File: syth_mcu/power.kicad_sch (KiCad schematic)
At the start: 31 parts, among them U3 AMS1117-3.3, U4 AMS1117-3.3

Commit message: All traces, no drc runs yet
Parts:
- U3, U4: footprint Package_TO_SOT_SMD:SOT-223-3_TabPin2 -> Package_TO_SOT_SMD:TO-252-3_TabPin2
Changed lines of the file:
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@@
 			)
 		)
-		(property "Footprint" "Package_TO_SOT_SMD:SOT-223-3_TabPin2"
+		(property "Footprint" "Package_TO_SOT_SMD:TO-252-3_TabPin2"
 			(at 46.99 105.41 0)
 			(hide yes)
@@
 			)
 		)
-		(property "Footprint" "Package_TO_SOT_SMD:SOT-223-3_TabPin2"
+		(property "Footprint" "Package_TO_SOT_SMD:TO-252-3_TabPin2"
 			(at 46.99 76.2 0)
 			(hide yes)

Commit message: Fixes from review 2
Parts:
- F1, F2: footprint Capacitor_THT:C_Disc_D5.1mm_W3.2mm_P5.00mm -> synth:RXEF040
- F3: footprint Capacitor_THT:C_Disc_D5.1mm_W3.2mm_P5.00mm -> synth:RXEF160
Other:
- note added: "AMS1 used for mux, and pot into gpio is neglegible, thus max current pulled is 50mA"
- note removed: "AMS1 used for mux, and pot into gpio is neglegible, thus max current pulled is 168mA"
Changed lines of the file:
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@@
 		)
 	)
-	(text "AMS1 used for mux,\nand pot into gpio is neglegible,\nthus max current pulled is 168mA"
+	(text "AMS1 used for mux,\nand pot into gpio is neglegible,\nthus max current pulled is 50mA"
 		(exclude_from_sim no)
 		(at 104.394 83.058 0)
@@
 			)
 		)
-		(property "Footprint" "Capacitor_THT:C_Disc_D5.1mm_W3.2mm_P5.00mm"
+		(property "Footprint" "synth:RXEF040"
 			(at 69.85 80.01 0)
 			(hide yes)
@@
 			)
 		)
-		(property "Footprint" "Capacitor_THT:C_Disc_D5.1mm_W3.2mm_P5.00mm"
+		(property "Footprint" "synth:RXEF160"
 			(at 60.96 25.4 0)
 			(hide yes)
@@
 			)
 		)
-		(property "Footprint" "Capacitor_THT:C_Disc_D5.1mm_W3.2mm_P5.00mm"
+		(property "Footprint" "synth:RXEF040"
 			(at 68.58 109.22 0)
 			(hide yes)

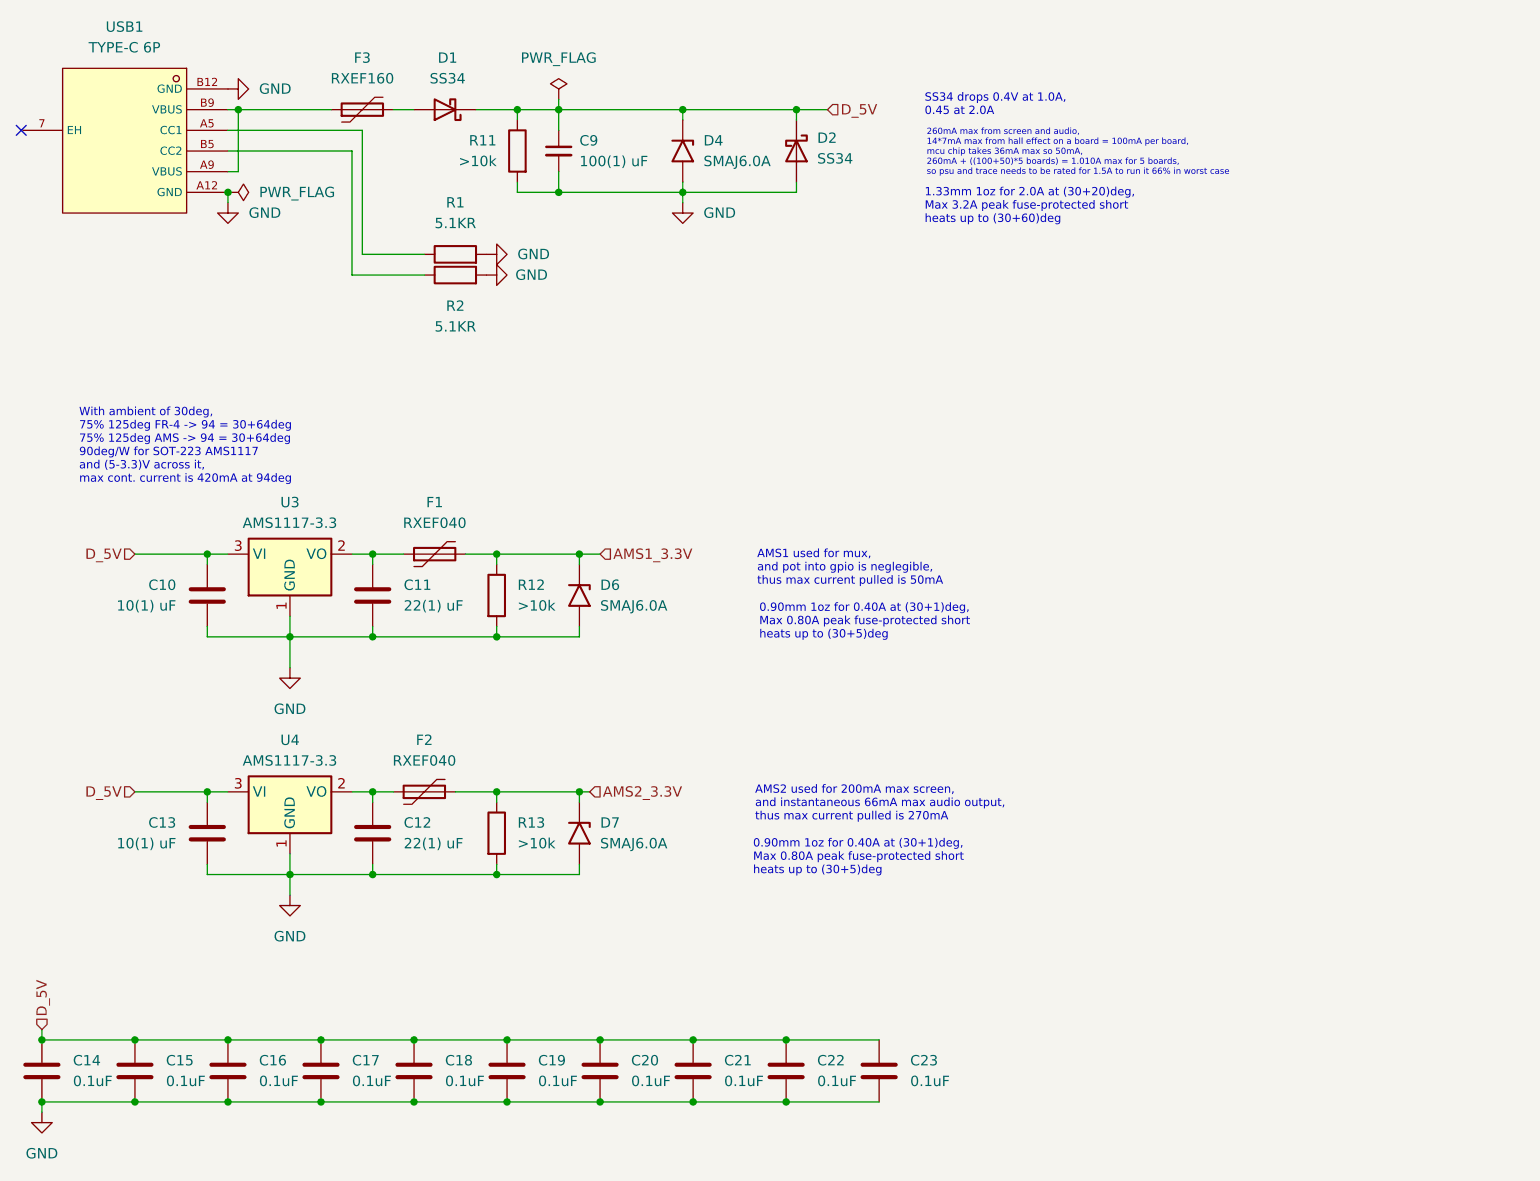
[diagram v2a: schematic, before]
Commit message: Unity-gain audio, merge AMS, 12 pots to mux, revs, footprint
Footprints:
- RXEF fuses with 1x dimension silkscreen and +0.2mm courtyard
- AMS1117 with 0.5mm minimum soldering space on all sides
- SS12D10 wider pins and add courtyard
- Changed orientation of AH3503 TO-92 to match datasheet
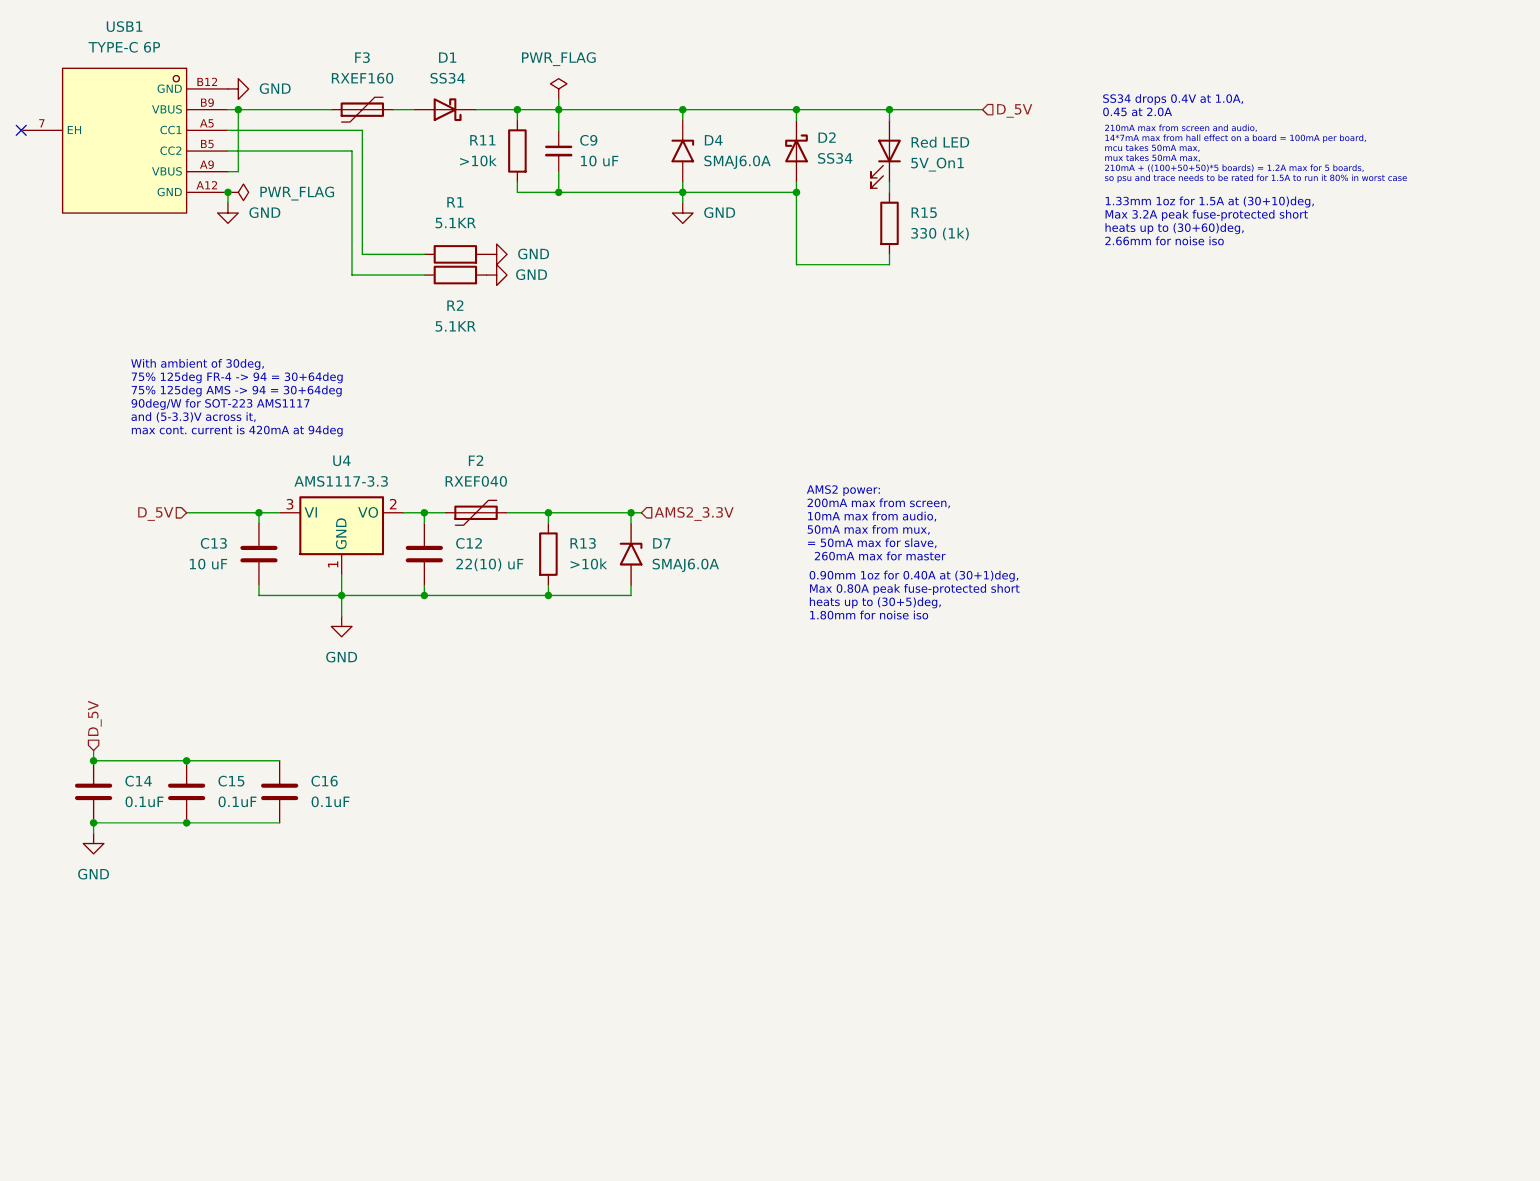
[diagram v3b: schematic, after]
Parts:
- removed C10: 10(1) uF, Capacitor_THT:C_Disc_D5.0mm_W2.5mm_P5.00mm, symbol Device:C
- removed C11: 22(1) uF, Capacitor_THT:C_Disc_D5.0mm_W2.5mm_P5.00mm, symbol Device:C
- removed C17, C18, C19, C20, C21, C22, C23: 0.1uF, Capacitor_THT:C_Disc_D5.0mm_W2.5mm_P5.00mm, symbol Device:C
- removed D6: SMAJ6.0A, Diode_SMD:D_SMA, symbol Diode:SMAJ5.0A
- removed F1: RXEF040, synth:RXEF040, symbol Device:Polyfuse
- removed R12: >10k, Resistor_THT:R_Axial_DIN0207_L6.3mm_D2.5mm_P10.16mm_Horizontal, symbol Device:R
- removed U3: AMS1117-3.3, Package_TO_SOT_SMD:TO-252-3_TabPin2, symbol Regulator_Linear:AMS1117-3.3
- added 5V_On1: Red LED, LED_THT:LED_D3.0mm, symbol Device:LED
- added R15: 330 (1k), Resistor_THT:R_Axial_DIN0207_L6.3mm_D2.5mm_P10.16mm_Horizontal, symbol Device:R
- C12: value 22(1) uF -> 22(10) uF; footprint Capacitor_THT:C_Disc_D5.0mm_W2.5mm_P5.00mm -> Capacitor_THT:CP_Radial_D4.0mm_P2.00mm
- C13: value 10(1) uF -> 10 uF; footprint Capacitor_THT:C_Disc_D5.0mm_W2.5mm_P5.00mm -> Capacitor_THT:CP_Radial_D4.0mm_P2.00mm
- C9: value 100(1) uF -> 10 uF; footprint Capacitor_THT:C_Disc_D5.0mm_W2.5mm_P5.00mm -> Capacitor_THT:CP_Radial_D4.0mm_P2.00mm
- U4: footprint Package_TO_SOT_SMD:TO-252-3_TabPin2 -> synth:TO-252-3_TabPin2_HandSolder
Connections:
- net D_5V: now also 5V_On1.2 (A)
- net GND: now also R15.2
- new net: 5V_On1.1 (K), R15.1
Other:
- note added: "0.90mm 1oz for 0.40A at (30+1)deg, Max 0.80A peak fuse-protected short heats up to (30+5)deg, 1.80mm for noise iso"
- note added: "1.33mm 1oz for 1.5A at (30+10)deg, Max 3.2A peak fuse-protected short heats up to (30+60)deg, 2.66mm for noise iso"
- note added: "210mA max from screen and audio, 14*7mA max from hall effect on a board = 100mA per board, mcu takes 50mA max, mux takes 50mA max, 210mA + ((100+50+50)*5 boards) = 1.2A max for 5 boards, so psu and trace needs to be rated for 1.5A to run it 80% in worst case"
- note added: "AMS2 power: 200mA max from screen, 10mA max from audio, 50mA max from mux, = 50mA max for slave, 260mA max for master"
- note removed: "0.90mm 1oz for 0.40A at (30+1)deg, Max 0.80A peak fuse-protected short heats up to (30+5)deg"
- note removed: "1.33mm 1oz for 2.0A at (30+20)deg, Max 3.2A peak fuse-protected short heats up to (30+60)deg"
- note removed: "260mA max from screen and audio, 14*7mA max from hall effect on a board = 100mA per board, mcu chip takes 36mA max so 50mA, 260mA + ((100+50)*5 boards) = 1.010A max for 5 boards, so psu and trace needs to be rated for 1.5A to run it 66% in worst case"
- note removed: "AMS1 used for mux, and pot into gpio is neglegible, thus max current pulled is 50mA"
- note removed: "AMS2 used for 200mA max screen, and instantaneous 66mA max audio output, thus max current pulled is 270mA"
- moved on the sheet: C12, C13, C14, C15, C16, D7, F2, R13, U4

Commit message: v2 schematic merge, power and signal routing
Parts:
- added AMS3.3VFused1, GND1, GND2, USB5VFused1: TestPoint, Connector_PinHeader_2.54mm:PinHeader_1x02_P2.54mm_Vertical, symbol Connector:TestPoint
- C12: value 22(10) uF -> 22(10)uF
- C13, C9: value 10 uF -> 10uF
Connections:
- net AMS2_3.3V: now also AMS3.3VFused1.1
- net D_5V: now also USB5VFused1.1
- net GND: now also GND1.1, GND2.1
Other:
- moved on the sheet: 5V_On1, D2, D4, R15

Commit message: System check, DRC runs
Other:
- note added: "210mA max from screen and audio, 14*12mA max from hall effect on a board = 168mA per board, mcu takes 50mA max, mux takes 50mA max, 210mA + ((168+50+50)*5 boards) = 1.550A max for 5 boards"
- note removed: "210mA max from screen and audio, 14*7mA max from hall effect on a board = 100mA per board, mcu takes 50mA max, mux takes 50mA max, 210mA + ((100+50+50)*5 boards) = 1.2A max for 5 boards, so psu and trace needs to be rated for 1.5A to run it 80% in worst case"
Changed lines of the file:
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@@
 		)
 	)
-	(text "210mA max from screen and audio,\n14*7mA max from hall effect on a board = 100mA per board,\nmcu takes 50mA max,\nmux takes 50mA max,\n210mA + ((100+50+50)*5 boards) = 1.2A max for 5 boards,\nso psu and trace needs to be rated for 1.5A to run it 80% in worst case"
+	(text "210mA max from screen and audio,\n14*12mA max from hall effect on a board = 168mA per board,\nmcu takes 50mA max,\nmux takes 50mA max,\n210mA + ((168+50+50)*5 boards) = 1.550A max for 5 boards"
 		(exclude_from_sim no)
 		(at 147.066 32.258 0)

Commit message: add screw, removed serial rev.pol diode
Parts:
- removed D1: SS34, Diode_SMD:D_SMA, symbol Diode:SS14
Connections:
- net D_5V: now also F3.2
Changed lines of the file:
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@@
 	(wire
 		(pts
-			(xy 62.23 26.67) (xy 59.69 26.67)
+			(xy 59.69 26.67) (xy 74.93 26.67)
 		)
 		(stroke
@@
 		(pts
 			(xy 74.93 26.67) (xy 80.01 26.67)
-		)
-		(stroke
-			(width 0)
-			(type default)
-		)
-	)
-	(wire
-		(pts
-			(xy 69.85 26.67) (xy 74.93 26.67)
 		)
 		(stroke
@@
 					(unit 1)
 				)
-			)
-		)
-	)
-	(symbol
-		(lib_id "Diode:SS14")
-		(at 66.04 26.67 180)
-		(unit 1)
-		(body_style 1)
-		(exclude_from_sim no)
-		(in_bom yes)
-		(on_board yes)
-		(in_pos_files yes)
-		(dnp no)
-		(fields_autoplaced yes)
-		(property "Reference" "D1"
-			(at 66.3575 20.32 0)
-			(show_name no)
-			(do_not_autoplace no)
-			(effects
-				(font
-					(size 1.27 1.27)
-				)
-			)
-		)
-		(property "Value" "SS34"
-			(at 66.3575 22.86 0)
-			(show_name no)
-			(do_not_autoplace no)
-			(effects
-				(font
-					(size 1.27 1.27)
-				)
-			)
-		)
-		(property "Footprint" "Diode_SMD:D_SMA"
-			(at 66.04 22.225 0)
-			(hide yes)
-			(show_name no)
-			(do_not_autoplace no)
-			(effects
-				(font
-					(size 1.27 1.27)
-				)
-			)
-		)
-		(property "Datasheet" "https://www.vishay.com/docs/88746/ss12.pdf"
-			(at 66.04 26.67 0)
-			(hide yes)
-			(show_name no)
-			(do_not_autoplace no)
-			(effects
-				(font
-					(size 1.27 1.27)
-				)
-			)
-		)
-		(property "Description" "40V 1A Schottky Diode, SMA"
-			(at 66.04 26.67 0)
-			(hide yes)
-			(show_name no)
-			(do_not_autoplace no)
-			(effects
-				(font
-					(size 1.27 1.27)
-				)
-			)
-		)
-		(pin "2"
-		)
-		(pin "1"
-		)
-		(instances
-			(project "syth_mcu"
-				(path "/6f6073ad-48fd-4b64-b32f-c8e9bfc21ddc/077ae08f-3ae9-40e2-a0fd-b215fa7f173f"
-					(reference "D1")
-					(unit 1)
-				)
